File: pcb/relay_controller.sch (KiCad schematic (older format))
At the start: 58 parts, among them P1 PWR_JACK_2.5x5.5, P10 HEADER_02X08_SMD, P11 HEADER_02X08_SMD, P2 HEADER_01X03_SMD_RA, P3 HEADER_01X03_SMD_RA, P4 HEADER_01X03_SMD_RA, P5 HEADER_01X03_SMD_RA, P6 HEADER_01X02_SMD_RA, P7 BNC_DOUBLE_RA, P8 HEADER_02X08_SMD, P9 HEADER_02X08_SMD, SW1 SPST_SLIDE_AS, U1 TLE7230R, U2 TLE7230R, U3 TLE7230R, U4 TLE7230R

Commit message: Progress towards pcb1.0.
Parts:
- removed C4, C5, C6, C7: 0.1uF, relay_controller:SM1210, symbol 0.1uF
- removed D1, D10, D11, D12, D13, D14, D15, D16, D17, D18, D19, D2, D20, D21, D22, D23, D24, D25, D26, D27, D28, D29, D3, D30, D31, D32, D33, D4, D5, D6, D7, D8, D9: LED_24V, relay_controller:LED_555-3XXX, symbol LED_24V
- removed P10, P11, P8, P9: HEADER_02X08_SMD, relay_controller:HEADER_02x08_SMD, symbol HEADER_02X08_SMD
- removed U1, U2, U3, U4: TLE7230R, relay_controller:PG-DSO-36, symbol TLE7230R
- added L?: LED_24V, relay_controller:LED_555-3XXX, symbol LED_24V
- added R?: 150, relay_controller:SM1210, symbol 150
- added T?: TERM_BLK_ANG_2_PIN, relay_controller:TERM_BLK_ANG_2_PIN, symbol TERM_BLK_ANG_2_PIN
- added U?: SSR_DC_6PIN, relay_controller:ASSR-1611, symbol SSR_DC_6PIN
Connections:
- net GND: now also L?.2 (K), U?.2 (-CTL)
- net LED_PWR: now also L?.1 (A)
- net CS: no longer names the net of ARDUINO1.46 (D46/PWM/OC5A/PL3)
- net MISO: no longer names the net of ARDUINO1.50 (D50/MISO/PCINT3/PB3)
- net MOSI: no longer names the net of ARDUINO1.51 (D51/MOSI/PCINT2/PB2)
- net RESET: no longer names the net of ARDUINO1.44 (D44/PWM/OC5C/PL5)
- net SCK: no longer names the net of ARDUINO1.52 (D52/SCK/PCINT1/PB1)
- new net: R?.1, U?.1 (+CTL)
- new net: T?.2 (P2), U?.4 (+LOAD)
- new net: T?.1 (P1), U?.6 (+LOAD)
- new net RELAY_0: R?.2
- no-connect marks 73 -> 71

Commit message: More progress towards pcb1.0.
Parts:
- added L2, L3, L4, L5, L6, L7, L8, L9: LED_5V_GRN, relay_controller:LED_555-3XXX, symbol LED_5V_GRN
- added R1: 5.11k, relay_controller:SM1210, symbol 5.11k
- added R10, R4, R5, R6, R7, R8, R9: 150, relay_controller:SM1210, symbol 150
- added R2: 1k, relay_controller:SM1210, symbol 1k
- added T2, T3, T4, T5, T6, T7, T8: TERM_BLK_ANG_2_PIN, relay_controller:TERM_BLK_ANG_2_PIN, symbol TERM_BLK_ANG_2_PIN
- added U2, U3, U4, U5, U6, U7, U8: SSR_DC_6PIN, relay_controller:ASSR-1611, symbol SSR_DC_6PIN
- gave numbers to parts that had none: 4
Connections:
- net GND: now also L2.2 (K), L3.2 (K), L4.2 (K), L5.2 (K), L6.2 (K), L7.2 (K), L8.2 (K), L9.2 (K), R2.2, U2.2 (-CTL), U3.2 (-CTL), U4.2 (-CTL), U5.2 (-CTL), U6.2 (-CTL), U7.2 (-CTL), U8.2 (-CTL)
- net LED_PWR: now also R1.1
- net RELAY_0: now also ARDUINO1.38 (D38/T0/PD7)
- net LED_0: now reaches ARDUINO1.22 (D22/AD0/PA0)
- net LED_0: now also L2.1 (A)
- net LED_1: now reaches ARDUINO1.23 (D23/AD1/PA1)
- net LED_1: now also L3.1 (A)
- net LED_2: now reaches ARDUINO1.24 (D24/AD2/PA2)
- net LED_2: now also L4.1 (A)
- net LED_3: now reaches ARDUINO1.25 (D25/AD3/PA3)
- net LED_3: now also L5.1 (A)
- net LED_4: now reaches ARDUINO1.26 (D26/AD4/PA4)
- net LED_4: now also L6.1 (A)
- net LED_5: now reaches ARDUINO1.27 (D27/AD5/PA5)
- net LED_5: now also L7.1 (A)
- net LED_6: now reaches ARDUINO1.28 (D28/AD6/PA6)
- net LED_6: now also L8.1 (A)
- net LED_7: now reaches ARDUINO1.29 (D29/AD7/PA7)
- net LED_7: now also L9.1 (A)
- net LED_PWR_IN: now reaches ARDUINO1.33 (D33/A12/PC4)
- net LED_PWR_IN: now also R1.2, R2.1
- net RELAY_1: now reaches ARDUINO1.39 (D39/ALE/PG2)
- net RELAY_1: now also R4.2
- net RELAY_2: now reaches ARDUINO1.40 (D40/RD/PG1)
- net RELAY_2: now also R5.2
- net RELAY_3: now reaches ARDUINO1.41 (D41/WR/PG0)
- net RELAY_3: now also R6.2
- net RELAY_4: now reaches ARDUINO1.42 (D42/PL7)
- net RELAY_4: now also R7.2
- net RELAY_5: now reaches ARDUINO1.43 (D43/PL6)
- net RELAY_5: now also R8.2
- net RELAY_6: now reaches ARDUINO1.44 (D44/PWM/OC5C/PL5)
- net RELAY_6: now also R9.2
- net RELAY_7: now reaches ARDUINO1.45 (D45/PWM/OC5B/PL4)
- net RELAY_7: now also R10.2
- net OUT_0+: now reaches U1.4 (+LOAD)
- net OUT_0+: now also T1.1 (P1), U1.6 (+LOAD); no longer T1.2 (P2)
- net OUT_0-: now reaches U1.5 (-LOAD)
- net OUT_0-: now also T1.2 (P2)
- new net: R4.1, U2.1 (+CTL)
- new net: R5.1, U3.1 (+CTL)
- new net: R6.1, U4.1 (+CTL)
- new net: R7.1, U5.1 (+CTL)
- new net: R8.1, U6.1 (+CTL)
- new net: R9.1, U7.1 (+CTL)
- new net: R10.1, U8.1 (+CTL)
- new net OUT_1+: T2.1 (P1), U2.4 (+LOAD), U2.6 (+LOAD)
- new net OUT_1-: T2.2 (P2), U2.5 (-LOAD)
- new net OUT_2+: T3.1 (P1), U3.4 (+LOAD), U3.6 (+LOAD)
- new net OUT_2-: T3.2 (P2), U3.5 (-LOAD)
- new net OUT_3+: T4.1 (P1), U4.4 (+LOAD), U4.6 (+LOAD)
- new net OUT_3-: T4.2 (P2), U4.5 (-LOAD)
- new net OUT_4+: T5.1 (P1), U5.4 (+LOAD), U5.6 (+LOAD)
- new net OUT_4-: T5.2 (P2), U5.5 (-LOAD)
- new net OUT_5+: T6.1 (P1), U6.4 (+LOAD), U6.6 (+LOAD)
- new net OUT_5-: T6.2 (P2), U6.5 (-LOAD)
- new net OUT_6+: T7.1 (P1), U7.4 (+LOAD), U7.6 (+LOAD)
- new net OUT_6-: T7.2 (P2), U7.5 (-LOAD)
- new net OUT_7+: T8.1 (P1), U8.4 (+LOAD), U8.6 (+LOAD)
- new net OUT_7-: T8.2 (P2), U8.5 (-LOAD)
- no-connect marks 71 -> 53
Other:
- moved on the sheet: C1, C2, C3, L1, P1, P2, P3, P4, P5, P6, P7, R3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

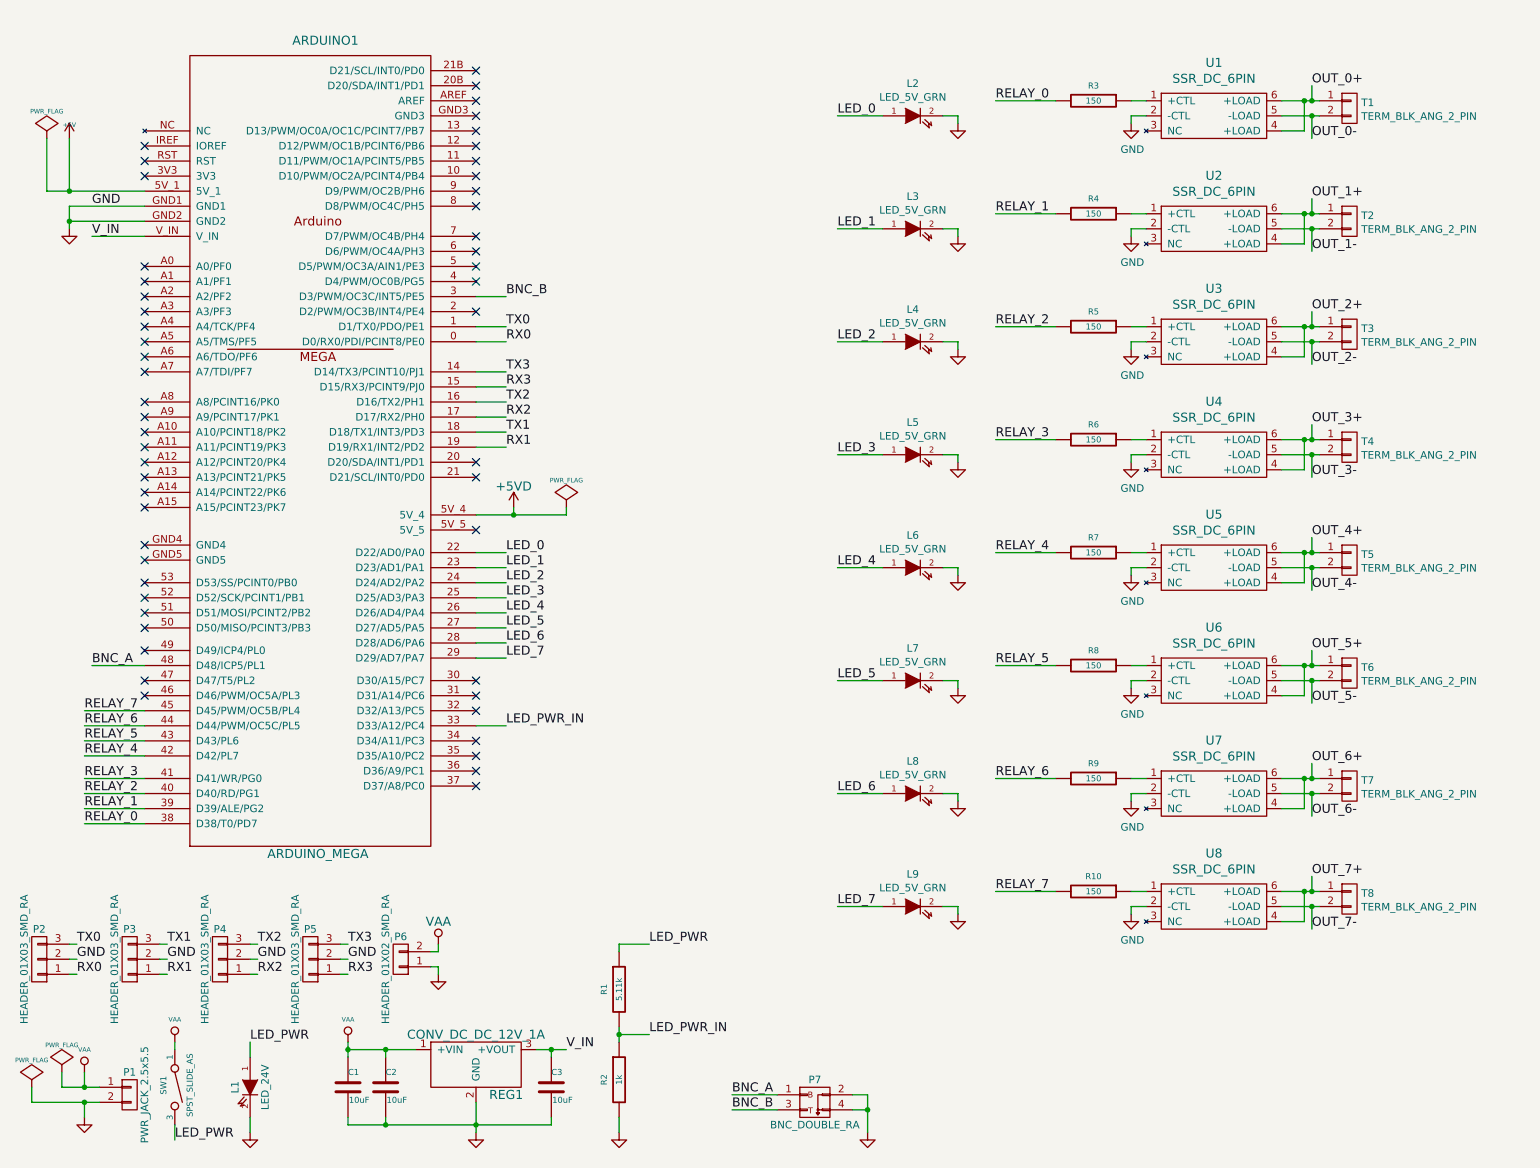
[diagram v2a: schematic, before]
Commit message: Switched LED_PWR to LED_GND.
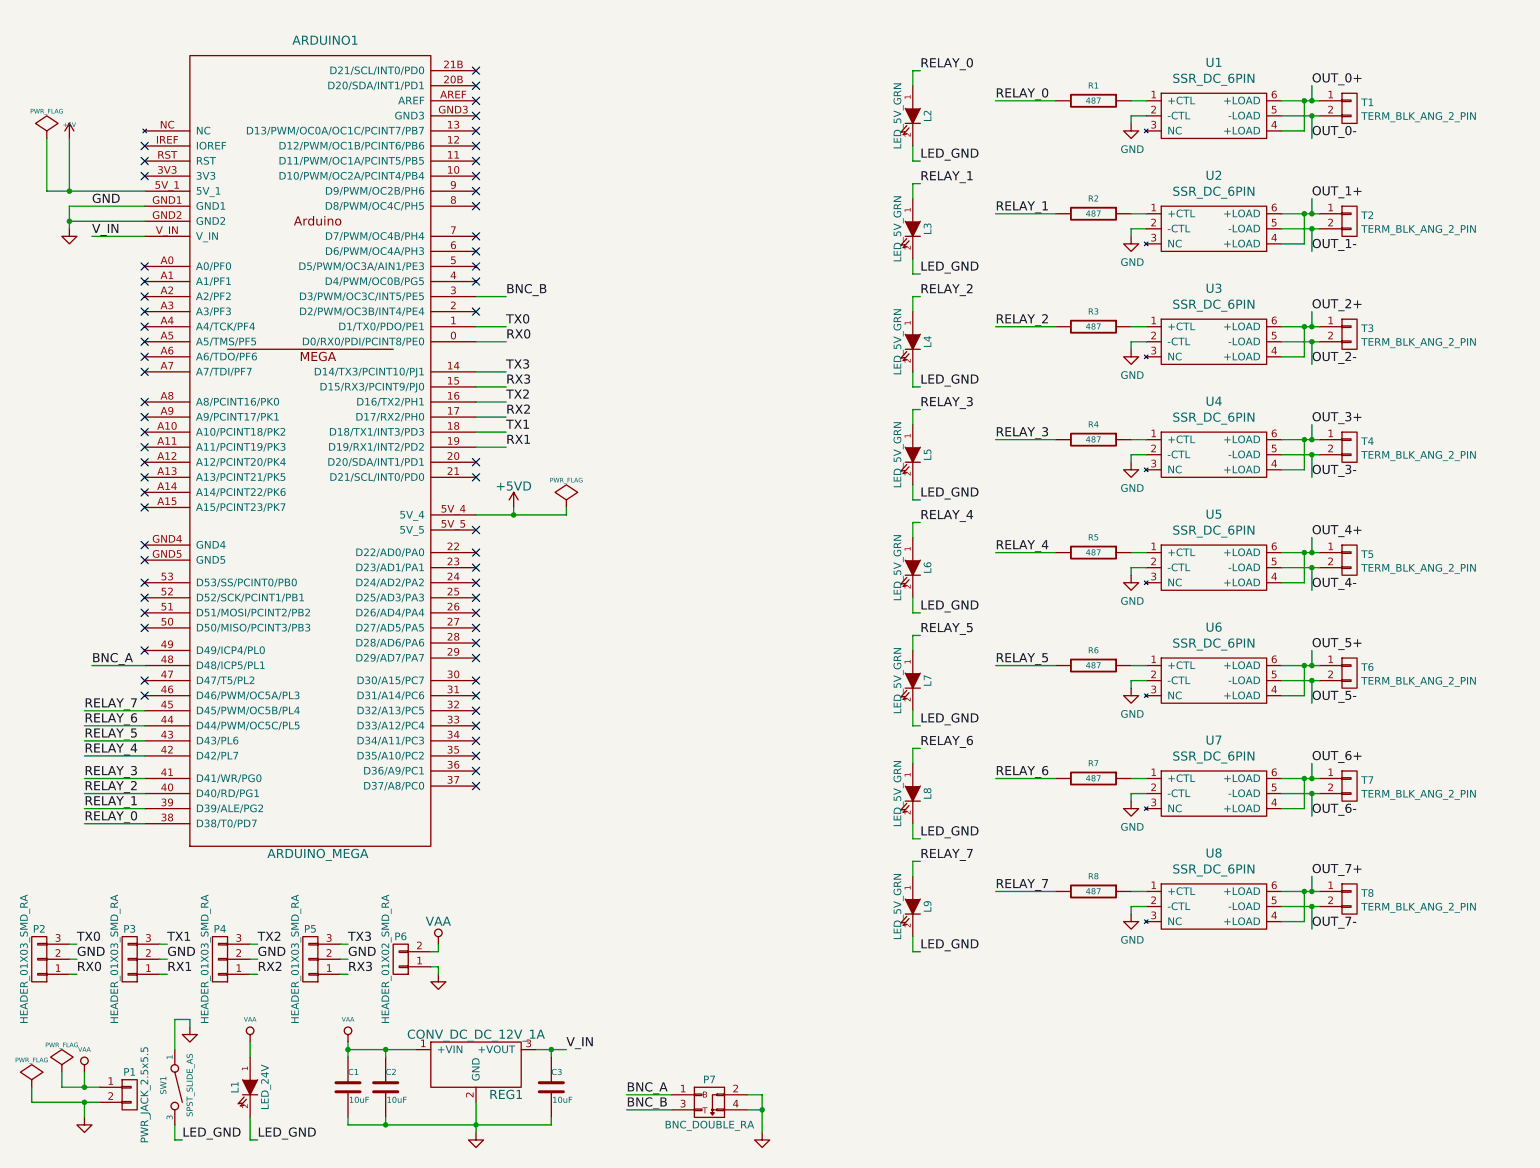
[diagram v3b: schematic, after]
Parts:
- removed R1: 5.11k, relay_controller:SM1210, symbol 5.11k
- removed R10, R3, R4, R5, R6, R7, R8, R9: 150, relay_controller:SM1210, symbol 150
- removed R2: 1k, relay_controller:SM1210, symbol 1k
- added R1, R2, R3, R4, R5, R6, R7, R8: 487, relay_controller:SM1210, symbol 487
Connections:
- net GND: now also SW1.1; no longer L1.2 (K), L2.2 (K), L3.2 (K), L4.2 (K), L5.2 (K), L6.2 (K), L7.2 (K), L8.2 (K), L9.2 (K)
- net RELAY_0: now also L2.1 (A), R1.2
- net RELAY_1: now also L3.1 (A), R2.2
- net RELAY_2: now also L4.1 (A), R3.2
- net RELAY_3: now also L5.1 (A), R4.2
- net RELAY_4: now also L6.1 (A), R5.2
- net RELAY_5: now also L7.1 (A), R6.2
- net RELAY_6: now also L8.1 (A), R7.2
- net RELAY_7: now also L9.1 (A), R8.2
- net VAA: now also L1.1 (A); no longer SW1.1
- net at U1.1 (+CTL): now also R1.1
- net at U2.1 (+CTL): now also R2.1
- net at U3.1 (+CTL): now also R3.1
- net at U4.1 (+CTL): now also R4.1
- net at U5.1 (+CTL): now also R5.1
- net at U6.1 (+CTL): now also R6.1
- net at U7.1 (+CTL): now also R7.1
- net at U8.1 (+CTL): now also R8.1
- net LED_0: no longer names the net of ARDUINO1.22 (D22/AD0/PA0)
- net LED_0: no longer L2.1 (A)
- net LED_1: no longer names the net of ARDUINO1.23 (D23/AD1/PA1)
- net LED_1: no longer L3.1 (A)
- net LED_2: no longer names the net of ARDUINO1.24 (D24/AD2/PA2)
- net LED_2: no longer L4.1 (A)
- net LED_3: no longer names the net of ARDUINO1.25 (D25/AD3/PA3)
- net LED_3: no longer L5.1 (A)
- net LED_4: no longer names the net of ARDUINO1.26 (D26/AD4/PA4)
- net LED_4: no longer L6.1 (A)
- net LED_5: no longer names the net of ARDUINO1.27 (D27/AD5/PA5)
- net LED_5: no longer L7.1 (A)
- net LED_6: no longer names the net of ARDUINO1.28 (D28/AD6/PA6)
- net LED_6: no longer L8.1 (A)
- net LED_7: no longer names the net of ARDUINO1.29 (D29/AD7/PA7)
- net LED_7: no longer L9.1 (A)
- net LED_PWR renamed LED_GND
- net LED_GND: now also L1.2 (K), L2.2 (K), L3.2 (K), L4.2 (K), L5.2 (K), L6.2 (K), L7.2 (K), L8.2 (K), L9.2 (K); no longer L1.1 (A)
- net LED_PWR_IN: no longer names the net of ARDUINO1.33 (D33/A12/PC4)
- no-connect marks 53 -> 62
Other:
- moved on the sheet: P7

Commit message: Made changes to 1.1, must complete before manufacturing boards.
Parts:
- removed R1, R2, R3, R4, R5, R6, R7, R8: 487, relay_controller:SM1210, symbol 487
- added R1, R2, R3, R4, R5, R6, R7, R8: 249, relay_controller:SM1210, symbol 249
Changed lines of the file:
@@
 NoConn ~ 3550 1000
 NoConn ~ 3550 1100
-NoConn ~ 3550 1300
-NoConn ~ 3550 1400
-NoConn ~ 3550 1600
 NoConn ~ 3550 2000
 NoConn ~ 3550 2100
@@
 $EndComp
 NoConn ~ 1350 2200
-NoConn ~ 3550 1700
 NoConn ~ 3550 1900
 Wire Wire Line
@@
 Wire Wire Line
 	3550 2300 3750 2300
-NoConn ~ 3550 1500
 NoConn ~ 3550 5050
 Wire Wire Line
@@
 NoConn ~ 1350 4400
 NoConn ~ 1350 4500
-NoConn ~ 1350 4950
 $Comp
 L LED_24V L1
@@
 	9050 1200 9050 1000
 Connection ~ 9050 1000
-Wire Wire Line
-	1350 5050 950  5050
-Wire Wire Line
-	1350 5150 950  5150
-Wire Wire Line
-	1350 5250 950  5250
-Wire Wire Line
-	1350 5350 950  5350
-Wire Wire Line
-	1350 5500 950  5500
-Wire Wire Line
-	1350 5600 950  5600
-Wire Wire Line
-	1350 5700 950  5700
-Wire Wire Line
-	1350 5800 950  5800
-Text Label 950  5800 0    60   ~ 0
+Text Label 3750 1700 0    60   ~ 0
 RELAY_0
-Text Label 950  5700 0    60   ~ 0
+Text Label 3750 1600 0    60   ~ 0
 RELAY_1
-Text Label 950  5600 0    60   ~ 0
+Text Label 3750 1500 0    60   ~ 0
 RELAY_2
-Text Label 950  5500 0    60   ~ 0
+Text Label 3750 1400 0    60   ~ 0
 RELAY_3
-Text Label 950  5350 0    60   ~ 0
+Text Label 3750 1300 0    60   ~ 0
 RELAY_4
-Text Label 950  5250 0    60   ~ 0
+Text Label 950  5150 0    60   ~ 0
 RELAY_5
-Text Label 950  5150 0    60   ~ 0
+Text Label 950  5050 0    60   ~ 0
 RELAY_6
-Text Label 950  5050 0    60   ~ 0
+Text Label 950  4950 0    60   ~ 0
 RELAY_7
 Wire Wire Line
@@
 Text Label 6500 6650 0    60   ~ 0
 LED_GND
-$Comp
-L 487 R1
-U 1 1 57086194
+Wire Wire Line
+	3550 1700 3750 1700
+Wire Wire Line
+	3550 1600 3750 1600
+Wire Wire Line
+	3550 1500 3750 1500
+Wire Wire Line
+	3550 1400 3750 1400
+Wire Wire Line
+	3550 1300 3750 1300
+Wire Wire Line
+	1350 4950 950  4950
+Wire Wire Line
+	1350 5050 950  5050
+Wire Wire Line
+	1350 5150 950  5150
+NoConn ~ 1350 5250
+NoConn ~ 1350 5350
+NoConn ~ 1350 5500
+NoConn ~ 1350 5600
+NoConn ~ 1350 5700
+NoConn ~ 1350 5800
+$Comp
+L 249 R1
+U 1 1 571E5ECE
 P 7650 1000
 F 0 "R1" V 7550 1000 40  0000 C CNN
-F 1 "487" V 7650 1000 40  0000 C CNN
+F 1 "249" V 7650 1000 40  0000 C CNN
 F 2 "relay_controller:SM1210" V 7580 1000 30  0001 C CNN
 F 3 "" V 7730 1000 30  0000 C CNN
 F 4 "digikey" V 7830 1100 60  0001 C CNN "Vendor"
-F 5 "P487AACT-ND" V 7930 1200 60  0001 C CNN "PartNumber"
-F 6 "RES SMD 487 OHM 1% 1/2W 1210" V 8030 1300 60  0001 C CNN "Description"
+F 5 "P249AACT-ND" V 7930 1200 60  0001 C CNN "PartNumber"
+F 6 "249 Ohm 1% 0.5W 1210" V 8030 1300 60  0001 C CNN "Description"
 	1    7650 1000
 	0    1    1    0
 $EndComp
 $Comp
-L 487 R2
-U 1 1 5708667C
+L 249 R2
+U 1 1 571E6352
 P 7650 1750
 F 0 "R2" V 7550 1750 40  0000 C CNN
-F 1 "487" V 7650 1750 40  0000 C CNN
+F 1 "249" V 7650 1750 40  0000 C CNN
 F 2 "relay_controller:SM1210" V 7580 1750 30  0001 C CNN
 F 3 "" V 7730 1750 30  0000 C CNN
 F 4 "digikey" V 7830 1850 60  0001 C CNN "Vendor"
-F 5 "P487AACT-ND" V 7930 1950 60  0001 C CNN "PartNumber"
-F 6 "RES SMD 487 OHM 1% 1/2W 1210" V 8030 2050 60  0001 C CNN "Description"
+F 5 "P249AACT-ND" V 7930 1950 60  0001 C CNN "PartNumber"
+F 6 "249 Ohm 1% 0.5W 1210" V 8030 2050 60  0001 C CNN "Description"
 	1    7650 1750
 	0    1    1    0
 $EndComp
 $Comp
-L 487 R3
-U 1 1 57086752
+L 249 R3
+U 1 1 571E63FC
 P 7650 2500
 F 0 "R3" V 7550 2500 40  0000 C CNN
-F 1 "487" V 7650 2500 40  0000 C CNN
+F 1 "249" V 7650 2500 40  0000 C CNN
 F 2 "relay_controller:SM1210" V 7580 2500 30  0001 C CNN
 F 3 "" V 7730 2500 30  0000 C CNN
 F 4 "digikey" V 7830 2600 60  0001 C CNN "Vendor"
-F 5 "P487AACT-ND" V 7930 2700 60  0001 C CNN "PartNumber"
-F 6 "RES SMD 487 OHM 1% 1/2W 1210" V 8030 2800 60  0001 C CNN "Description"
+F 5 "P249AACT-ND" V 7930 2700 60  0001 C CNN "PartNumber"
+F 6 "249 Ohm 1% 0.5W 1210" V 8030 2800 60  0001 C CNN "Description"
 	1    7650 2500
 	0    1    1    0
 $EndComp
 $Comp
-L 487 R4
-U 1 1 570868F4
+L 249 R4
+U 1 1 571E64A7
 P 7650 3250
 F 0 "R4" V 7550 3250 40  0000 C CNN
-F 1 "487" V 7650 3250 40  0000 C CNN
+F 1 "249" V 7650 3250 40  0000 C CNN
 F 2 "relay_controller:SM1210" V 7580 3250 30  0001 C CNN
 F 3 "" V 7730 3250 30  0000 C CNN
 F 4 "digikey" V 7830 3350 60  0001 C CNN "Vendor"
-F 5 "P487AACT-ND" V 7930 3450 60  0001 C CNN "PartNumber"
-F 6 "RES SMD 487 OHM 1% 1/2W 1210" V 8030 3550 60  0001 C CNN "Description"
+F 5 "P249AACT-ND" V 7930 3450 60  0001 C CNN "PartNumber"
+F 6 "249 Ohm 1% 0.5W 1210" V 8030 3550 60  0001 C CNN "Description"
 	1    7650 3250
 	0    1    1    0
 $EndComp
 $Comp
-L 487 R5
-U 1 1 570869A8
+L 249 R5
+U 1 1 571E6701
 P 7650 4000
 F 0 "R5" V 7550 4000 40  0000 C CNN
-F 1 "487" V 7650 4000 40  0000 C CNN
+F 1 "249" V 7650 4000 40  0000 C CNN
 F 2 "relay_controller:SM1210" V 7580 4000 30  0001 C CNN
 F 3 "" V 7730 4000 30  0000 C CNN
 F 4 "digikey" V 7830 4100 60  0001 C CNN "Vendor"
-F 5 "P487AACT-ND" V 7930 4200 60  0001 C CNN "PartNumber"
-F 6 "RES SMD 487 OHM 1% 1/2W 1210" V 8030 4300 60  0001 C CNN "Description"
+F 5 "P249AACT-ND" V 7930 4200 60  0001 C CNN "PartNumber"
+F 6 "249 Ohm 1% 0.5W 1210" V 8030 4300 60  0001 C CNN "Description"
 	1    7650 4000
 	0    1    1    0
 $EndComp
 $Comp
-L 487 R6
-U 1 1 57086BB3
+L 249 R6
+U 1 1 571E69EB
 P 7650 4750
 F 0 "R6" V 7550 4750 40  0000 C CNN
-F 1 "487" V 7650 4750 40  0000 C CNN
+F 1 "249" V 7650 4750 40  0000 C CNN
 F 2 "relay_controller:SM1210" V 7580 4750 30  0001 C CNN
 F 3 "" V 7730 4750 30  0000 C CNN
 F 4 "digikey" V 7830 4850 60  0001 C CNN "Vendor"
-F 5 "P487AACT-ND" V 7930 4950 60  0001 C CNN "PartNumber"
-F 6 "RES SMD 487 OHM 1% 1/2W 1210" V 8030 5050 60  0001 C CNN "Description"
+F 5 "P249AACT-ND" V 7930 4950 60  0001 C CNN "PartNumber"
+F 6 "249 Ohm 1% 0.5W 1210" V 8030 5050 60  0001 C CNN "Description"
 	1    7650 4750
 	0    1    1    0
 $EndComp
 $Comp
-L 487 R7
-U 1 1 57086C6F
+L 249 R7
+U 1 1 571E6AA5
 P 7650 5500
 F 0 "R7" V 7550 5500 40  0000 C CNN
-F 1 "487" V 7650 5500 40  0000 C CNN
+F 1 "249" V 7650 5500 40  0000 C CNN
 F 2 "relay_controller:SM1210" V 7580 5500 30  0001 C CNN
 F 3 "" V 7730 5500 30  0000 C CNN
 F 4 "digikey" V 7830 5600 60  0001 C CNN "Vendor"
-F 5 "P487AACT-ND" V 7930 5700 60  0001 C CNN "PartNumber"
-F 6 "RES SMD 487 OHM 1% 1/2W 1210" V 8030 5800 60  0001 C CNN "Description"
+F 5 "P249AACT-ND" V 7930 5700 60  0001 C CNN "PartNumber"
+F 6 "249 Ohm 1% 0.5W 1210" V 8030 5800 60  0001 C CNN "Description"
 	1    7650 5500
 	0    1    1    0
 $EndComp
 $Comp
-L 487 R8
-U 1 1 57086D44
+L 249 R8
+U 1 1 571E6D28
 P 7650 6250
 F 0 "R8" V 7550 6250 40  0000 C CNN
-F 1 "487" V 7650 6250 40  0000 C CNN
+F 1 "249" V 7650 6250 40  0000 C CNN
 F 2 "relay_controller:SM1210" V 7580 6250 30  0001 C CNN
 F 3 "" V 7730 6250 30  0000 C CNN
 F 4 "digikey" V 7830 6350 60  0001 C CNN "Vendor"
-F 5 "P487AACT-ND" V 7930 6450 60  0001 C CNN "PartNumber"
-F 6 "RES SMD 487 OHM 1% 1/2W 1210" V 8030 6550 60  0001 C CNN "Description"
+F 5 "P249AACT-ND" V 7930 6450 60  0001 C CNN "PartNumber"
+F 6 "249 Ohm 1% 0.5W 1210" V 8030 6550 60  0001 C CNN "Description"
 	1    7650 6250
 	0    1    1    0
